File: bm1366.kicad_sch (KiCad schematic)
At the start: 78 parts, among them J2 Conn_01x06, U19 BM1370_mode1, U20 BM1370_mode1, U25 BM1370_mode1, U26 BM1370_mode1, U35 TXU0304PW, U8 25MHz

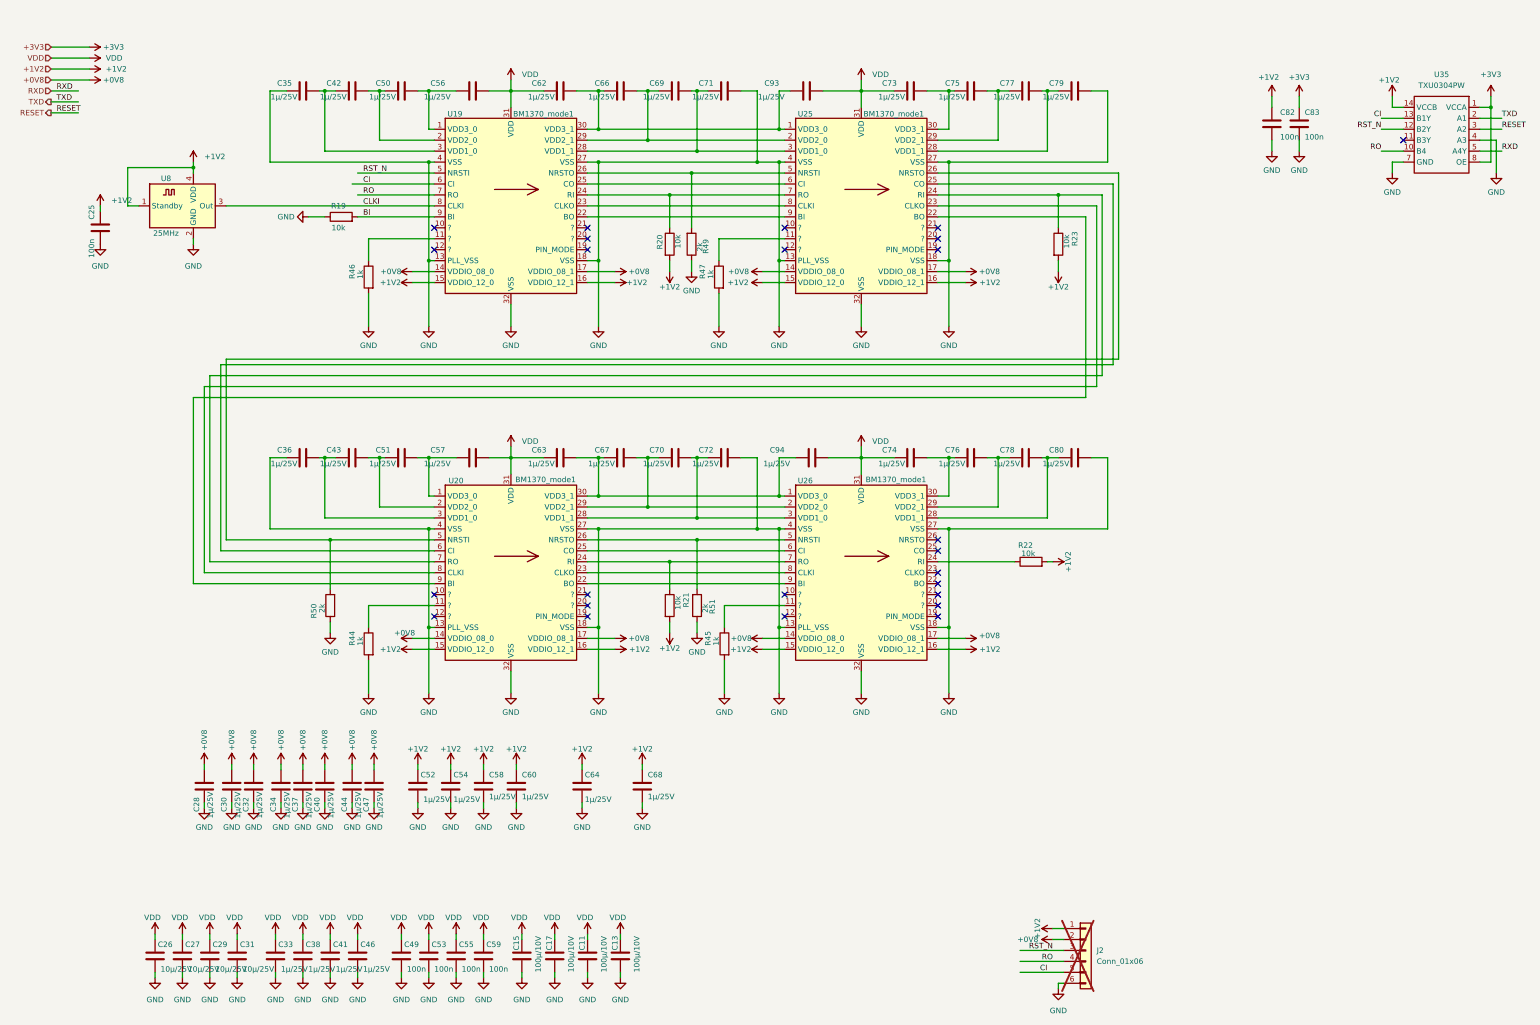
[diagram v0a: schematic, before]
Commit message: updated power stage placements
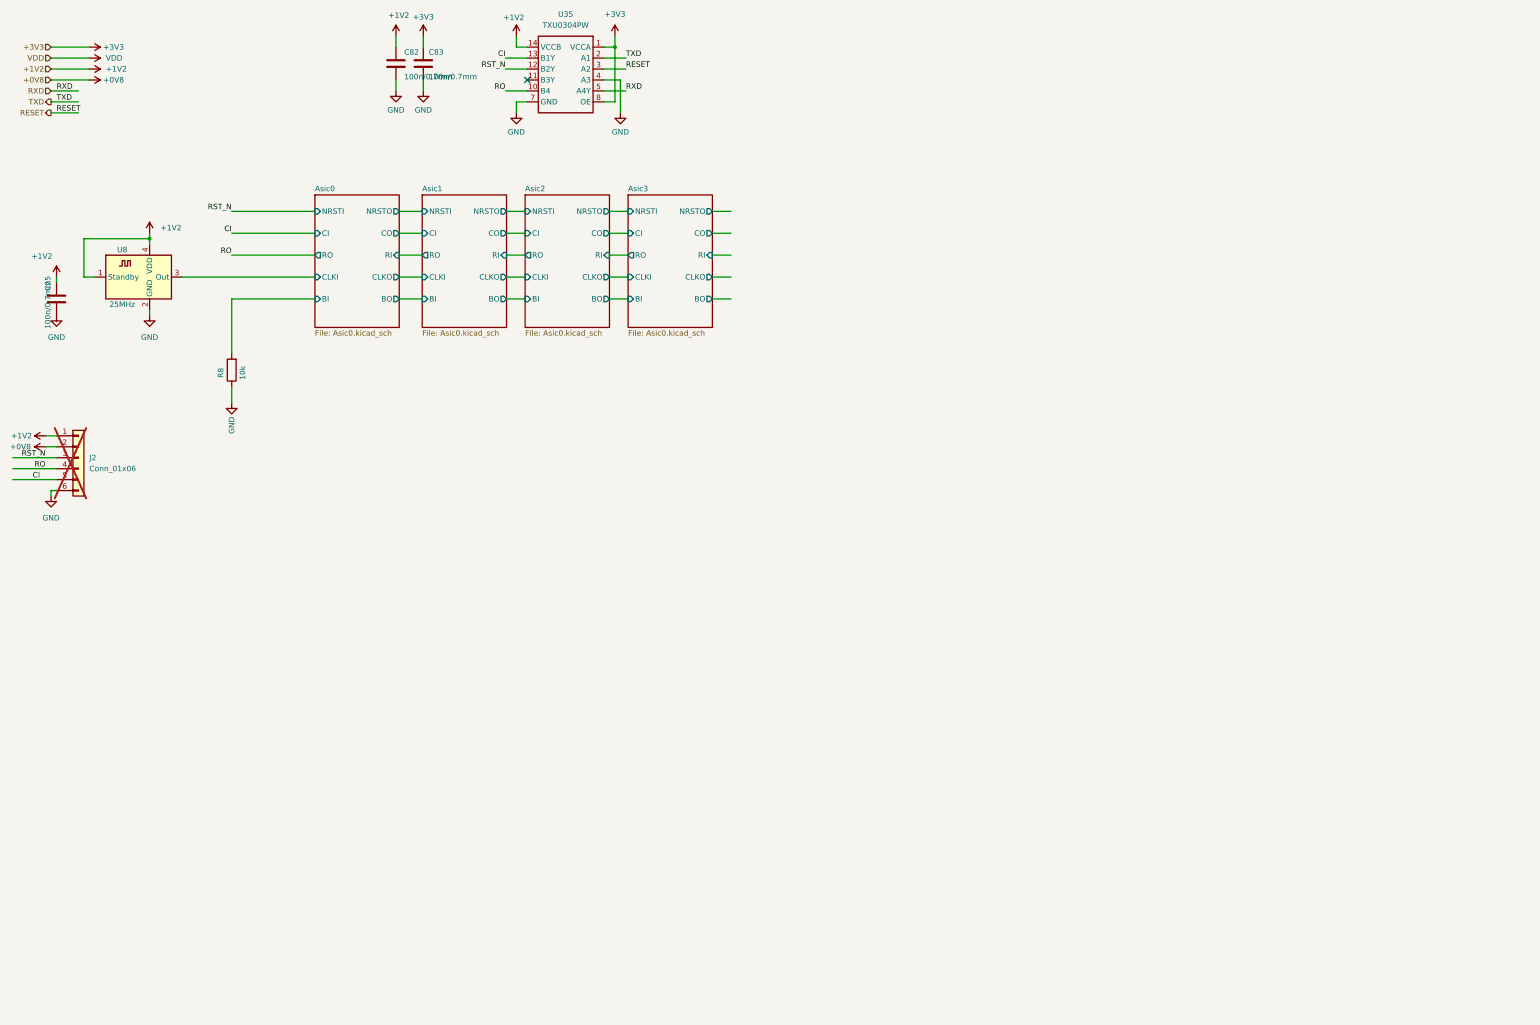
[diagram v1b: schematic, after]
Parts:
- removed C11, C13, C15, C17: 100µ/10V, Capacitor_SMD:C_1210_3225Metric, symbol Device:C
- removed C26, C27, C29, C31: 10µ/25V, Capacitor_SMD:C_0805_2012Metric, symbol Device:C
- removed C28, C30, C32, C33, C34, C35, C36, C37, C38, C40, C41, C42, C43, C44, C46, C47, C50, C51, C52, C54, C56, C57, C58, C60, C62, C63, C64, C66, C67, C68, C69, C70, C71, C72, C73, C74, C75, C76, C77, C78, C79, C80, C93, C94: 1µ/25V, Capacitor_SMD:C_0805_2012Metric, symbol Device:C
- removed C49, C53, C55, C59: 100n, Capacitor_SMD:C_0805_2012Metric, symbol Device:C
- removed R19, R20, R21, R22, R23: 10k, Resistor_SMD:R_0805_2012Metric, symbol Device:R
- removed R44, R45, R46, R47: 1k, Resistor_SMD:R_0805_2012Metric, symbol Device:R
- removed R49, R50, R51: 2k, Resistor_SMD:R_0805_2012Metric, symbol Device:R
- removed U19, U20, U25, U26: BM1370_mode1, qaxe:BM1370_JB, symbol mylib7:BM1368_mode1
- added R8: 10k, Resistor_SMD:R_0805_2012Metric, symbol Device:R
- C25, C82, C83: value 100n -> 100n/0.7mm; Manufacturer C0805C104K5RACTU -> AC0805KRX7R9BB104; OrderNr 399-C0805C104K5RACTUCT-ND -> 311-3037-1-ND; temp-coefficient X7R -> (none)
- U35: footprint Package_SO:TSSOP-14_4.4x5mm_P0.65mm -> Package_SO:TSSOP-14-1EP_4.4x5mm_P0.65mm
- U8: Manufacturer LFSPXO076024REEL -> 1923-LFSPXO076024CT-ND
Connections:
- net GND: now also R8.1
- net CLKI renamed Asic0/CLKI
- new net Asic0/BI: R8.2
- no-connect marks 25 -> 1
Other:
- added sheet Asic0 (Asic0.kicad_sch)
- added sheet Asic1 (Asic0.kicad_sch)
- added sheet Asic2 (Asic0.kicad_sch)
- added sheet Asic3 (Asic0.kicad_sch)
- moved on the sheet: C25, C82, C83, J2, U35, U8

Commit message: power stage in place
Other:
- moved on the sheet: C25, C82, C83, J2, R8, U35, U8

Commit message: Add LCSC number to components
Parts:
- C25, C82, C83: LCSC (none) -> C694249
- R8: LCSC (none) -> C84376
- U35: LCSC (none) -> C4364118
- U8: LCSC (none) -> C9006

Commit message: Use only stock component and unified LCSC capacitor code
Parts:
- C25, C82, C83: LCSC C694249 -> C49678
- R8: LCSC C84376 -> C2907219
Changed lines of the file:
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@@
 			)
 		)
-		(property "LCSC" "C694249"
+		(property "LCSC" "C49678"
 			(at 133.096 55.88 0)
 			(hide yes)
@@
 			)
 		)
-		(property "LCSC" "C694249"
+		(property "LCSC" "C49678"
 			(at 48.006 110.49 90)
 			(hide yes)
@@
 			)
 		)
-		(property "LCSC" "C84376"
+		(property "LCSC" "C2907219"
 			(at 88.646 127 0)
 			(hide yes)
@@
 			)
 		)
-		(property "LCSC" "C694249"
+		(property "LCSC" "C49678"
 			(at 126.746 55.88 0)
 			(hide yes)
